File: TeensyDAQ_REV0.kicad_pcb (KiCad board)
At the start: 4 copper layers, 101.6 x 82.6 mm, 108 parts, among them U100 TPS56637RPAR, U101 INA226AIDGSR, U102 BNO055, U103 SN65HVD230DR, U104 DRV5032FBDBZR, Y100 ABS07-32.768KHZ-T

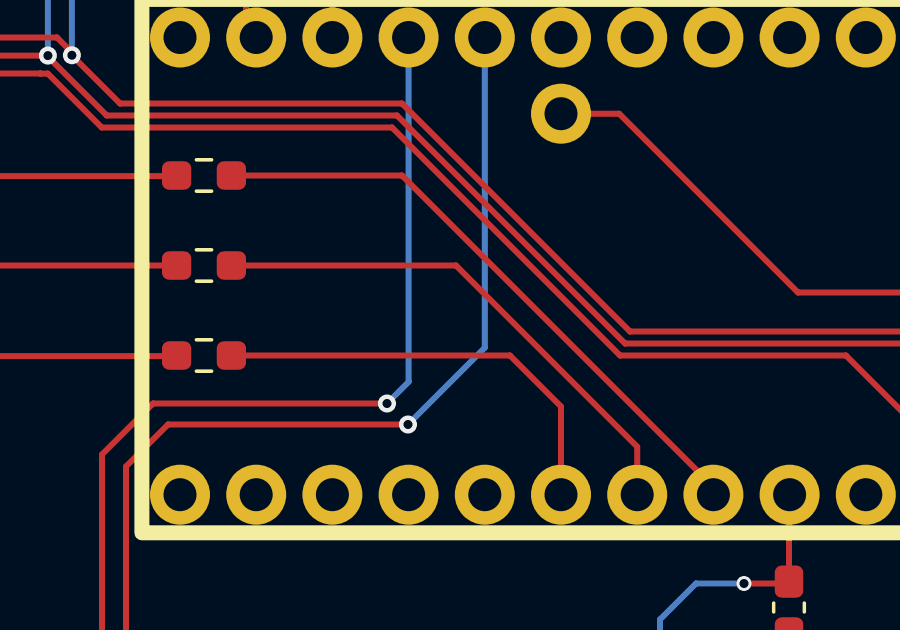
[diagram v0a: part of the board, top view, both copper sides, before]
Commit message: added gnd via to clean up copper pour
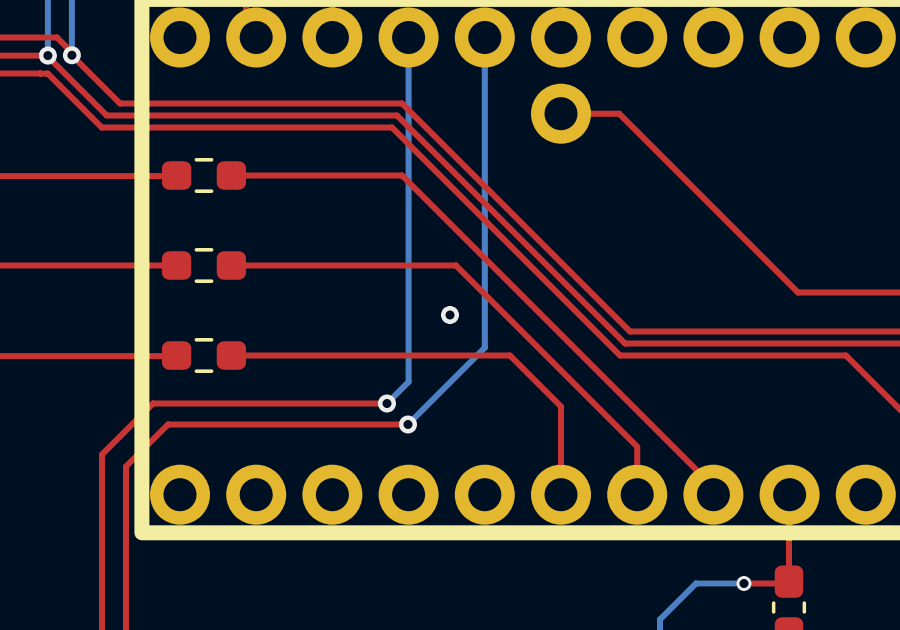
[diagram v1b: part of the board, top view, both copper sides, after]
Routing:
- net GND: vias 9 -> 10
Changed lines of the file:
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@@
+	)
+	(via
+		(at 146 93.25)
+		(size 0.6)
+		(drill 0.3)
+		(layers "F.Cu" "B.Cu")
+		(free yes)
+		(net 56)
 	)
 	(via
